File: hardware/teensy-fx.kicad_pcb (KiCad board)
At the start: 4 copper layers, 60 x 100 mm, 79 parts, among them J1 AudioJack3_Ground, J2 AudioJack3_Ground, J3 AudioJack3_Ground, SW1 Switch_SW_Push, SW2 Switch_SW_Push, SW3 Switch_SW_Push, SW4 Switch_SW_Push, U1 Teensy4.0, U2 AP7313-1.8V, U3 SGTL5000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

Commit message: try adding resistors to all the i2s lines
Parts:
- added RN1: R_Pack04, Resistor_SMD:R_Array_Convex_4x0603, F.Cu at (251.6, 55.2)
- moved R3 4.53 mm to (244.9, 54.0)
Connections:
- U3 pad 23: LRCLK -> Net-(RN1-Pad8)
- U3 pad 24: BCLK -> Net-(RN1-Pad7)
- U3 pad 25: I2S_IN -> Net-(RN1-Pad6)
- U3 pad 26: I2S_OUT -> Net-(RN1-Pad5)
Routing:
- net BCLK: track 17.8 -> 13.0 mm, vias 2 -> 0
- net LRCLK: track 17.6 -> 12.9 mm
- net MCLK: track 16.0 -> 11.9 mm
- net Net-(RN1-Pad5): track 0.00 -> 3.49 mm
- net Net-(R3-Pad1): track 5.99 -> 9.46 mm
- net Net-(RN1-Pad8): track 0.00 -> 3.46 mm
- net I2S_OUT: track 27.4 -> 24.0 mm
- net Net-(RN1-Pad7): track 0.00 -> 3.03 mm
- net Net-(RN1-Pad6): track 0.00 -> 2.95 mm
- net I2S_IN: track 22.2 -> 19.3 mm

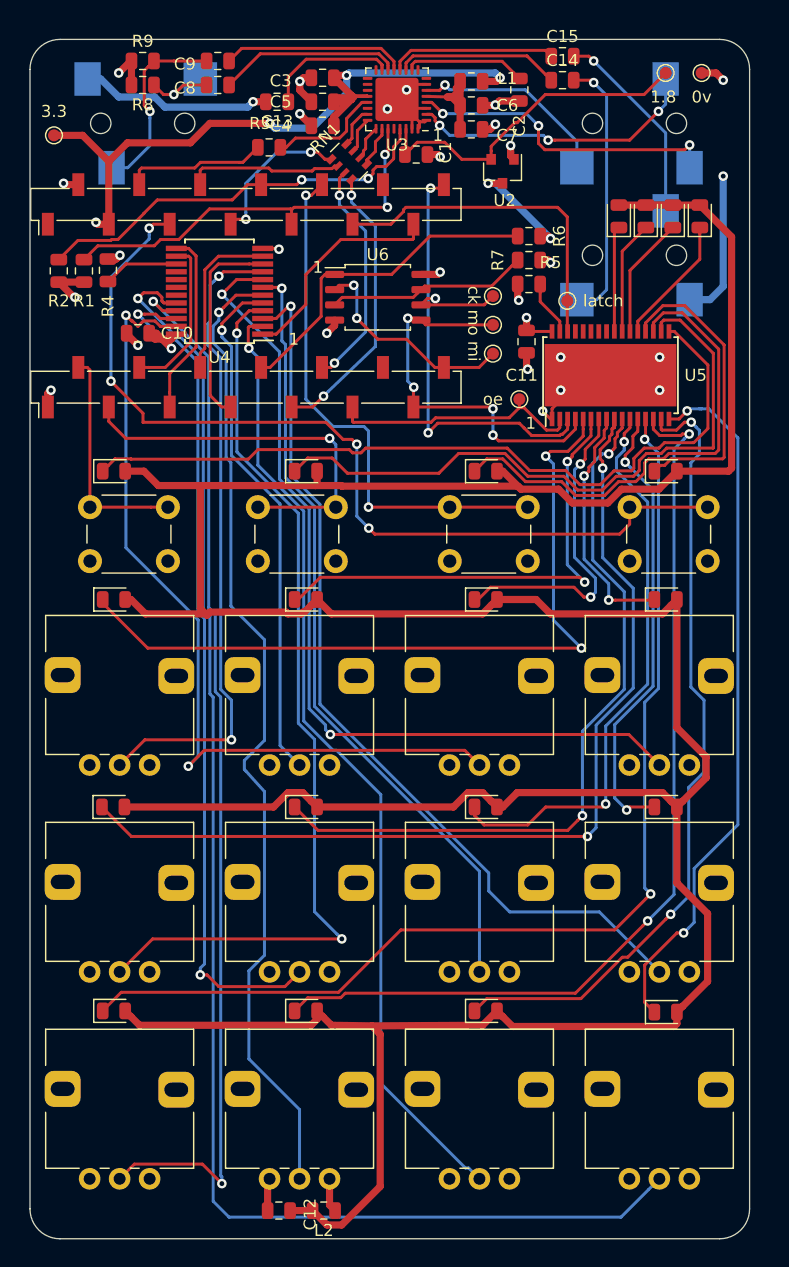
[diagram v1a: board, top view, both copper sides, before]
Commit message: change 3v3 plane to gnd, route all i2s signals on top plane, add rc filter for ADC pot input
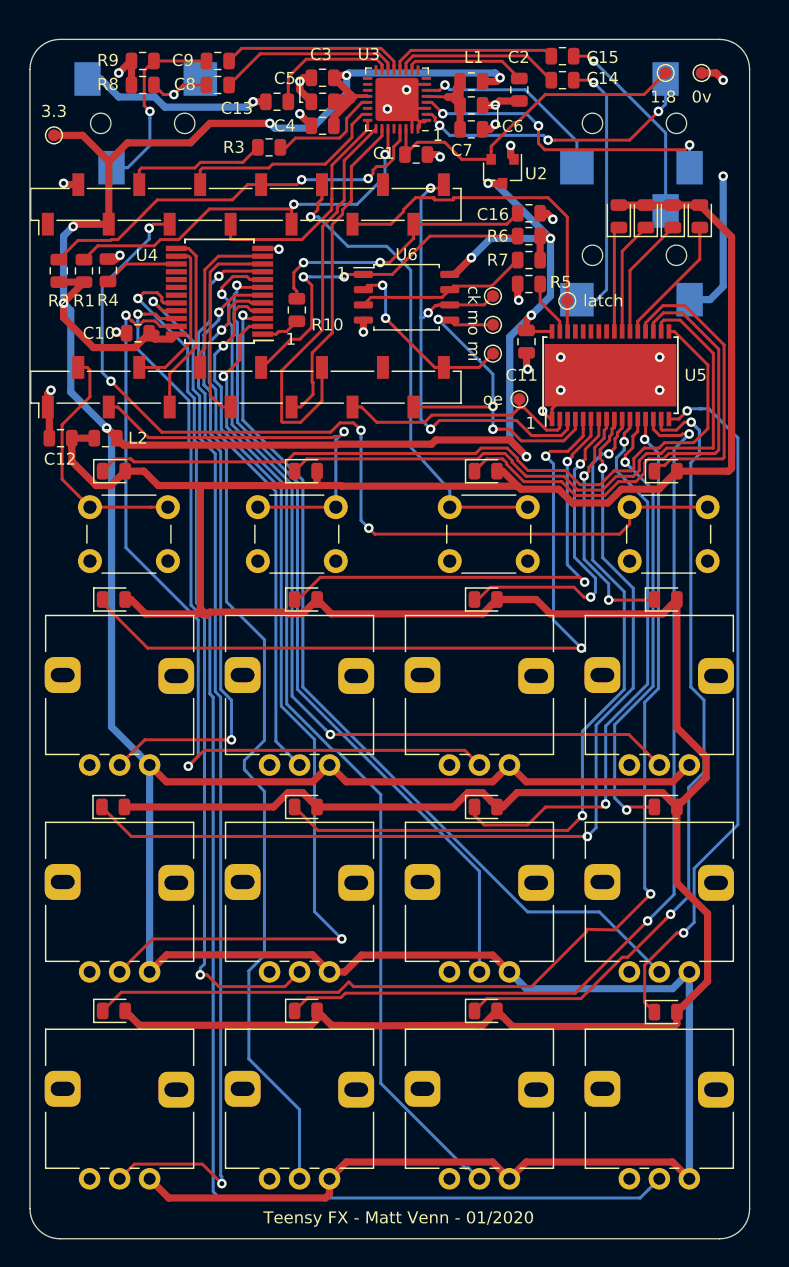
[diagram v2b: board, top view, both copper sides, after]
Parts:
- removed RN1: R_Pack04, Resistor_SMD:R_Array_Convex_4x0603
- added C16: 2.2uF, Capacitor_SMD:C_0805_2012Metric, F.Cu at (266.6, 59.5)
- added R10: 200r, Resistor_SMD:R_0805_2012Metric, F.Cu at (247.2, 67.6)
- moved C12 66.9 mm to (227.6, 78.2)
- moved L2 66.9 mm to (231.3, 78.2)
- moved U6 2.40 mm to (256.4, 66.5)
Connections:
- U3 pad 23: Net-(RN1-Pad8) -> BCLK
- U3 pad 24: Net-(RN1-Pad7) -> LRCLK
- U3 pad 25: Net-(RN1-Pad6) -> I2S_IN
- U3 pad 26: Net-(RN1-Pad5) -> I2S_OUT
- U4 pad 1: pot_multiplex -> Net-(R10-Pad1)
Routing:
- net +3V3: track 100.1 -> 395.9 mm
- net I2S_IN: track 19.3 -> 34.6 mm, vias 2 -> 0
- net +3.3VA: track 307.1 -> 293.7 mm
- net LRCLK: track 12.9 -> 19.4 mm, vias 2 -> 0
- net pot_multiplex: track 18.7 -> 23.7 mm, vias 0 -> 2
- net BCLK: track 13.0 -> 17.7 mm
- net sw_3: track 44.7 -> 40.8 mm, vias 2 -> 1
- net Net-(RN1-Pad5): track 3.49 -> 0.00 mm
- net Net-(R10-Pad1): track 0.00 -> 3.47 mm
- net Net-(RN1-Pad8): track 3.46 -> 0.00 mm
- net Net-(RN1-Pad7): track 3.03 -> 0.00 mm
- net Net-(RN1-Pad6): track 2.95 -> 0.00 mm
- net I2S_OUT: track 24.0 -> 26.8 mm, vias 2 -> 0
- net /pots buttons & LEDs/a2: track 65.5 -> 68.0 mm
- net /pots buttons & LEDs/a5: track 77.2 -> 79.8 mm
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- removed copper zone on In2.Cu, net +3V3
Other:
- board text added: "Teensy FX - Matt Venn - 01/2020"

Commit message: notes, check current, add extra decoupling cap for reg, move led supply to 5v
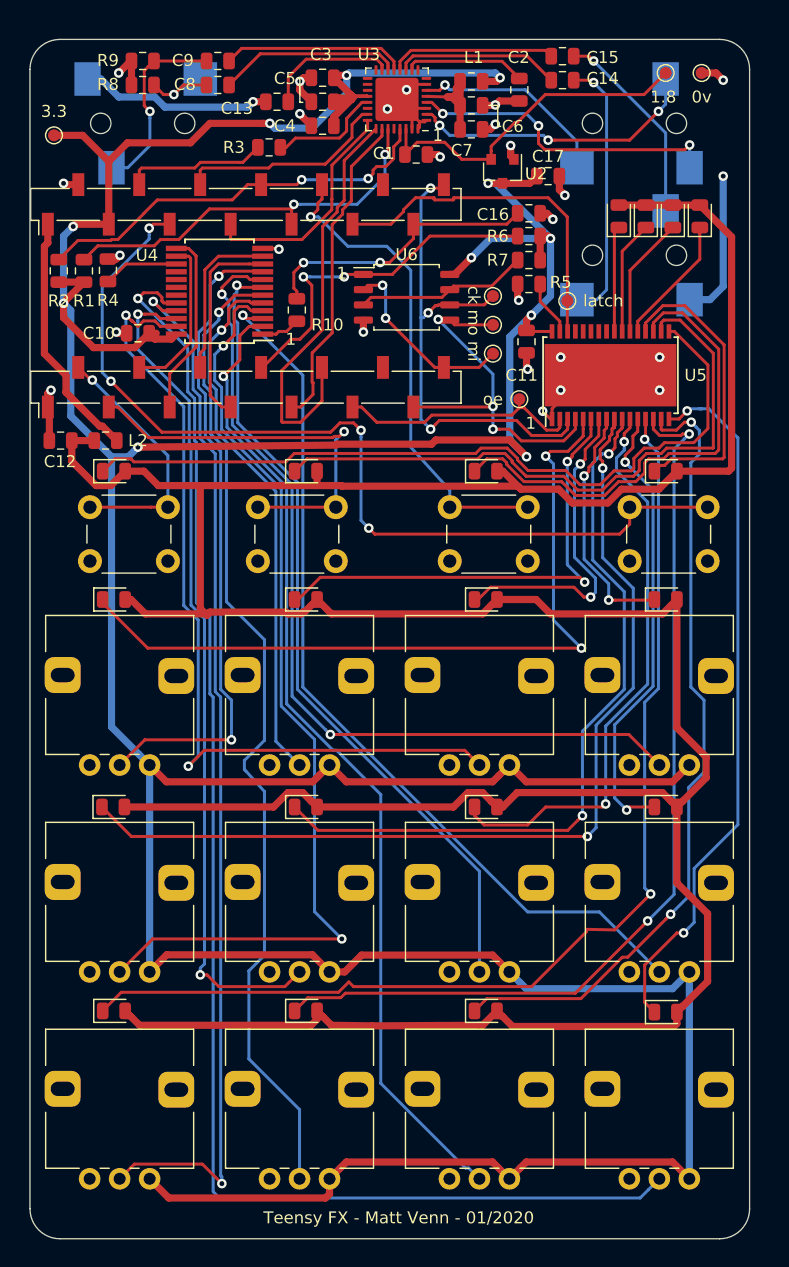
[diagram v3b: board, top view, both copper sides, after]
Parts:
- added C17: 2.2uF, Capacitor_SMD:C_0805_2012Metric, F.Cu at (268.2, 56.4)
- R5: value 3.3k -> 5k
- moved C12 0.20 mm to (227.6, 78.5)
- moved L2 0.20 mm to (231.3, 78.5)
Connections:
- net +3.3VA renamed +5VA
- L2 pad 1: +3V3 -> +5V
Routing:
- net +5V: track 0.00 -> 20.8 mm
- net +3V3: track 395.9 -> 398.3 mm
- net GND: track 80.3 -> 82.1 mm, vias 26 -> 27
- net sw_1: track 20.9 -> 21.3 mm, vias 0 -> 1

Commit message: fix teensy smt fp for molex part
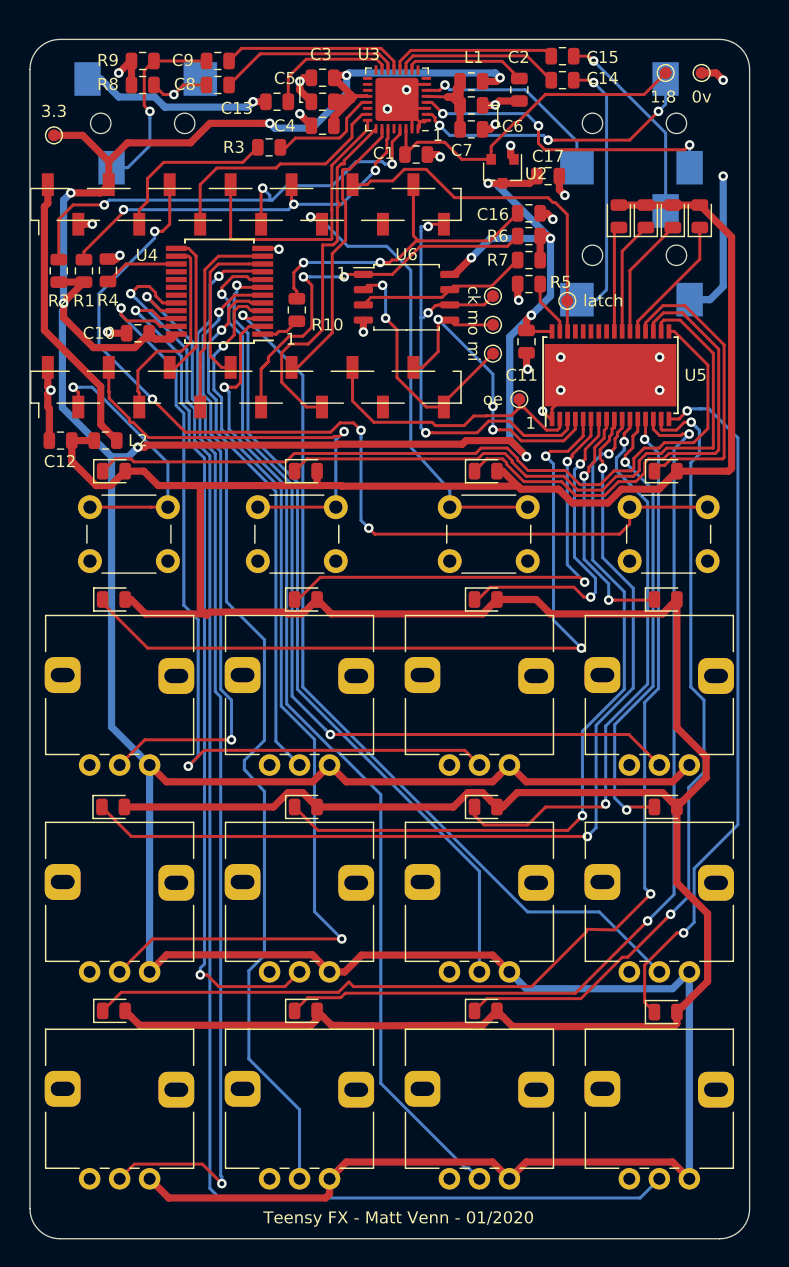
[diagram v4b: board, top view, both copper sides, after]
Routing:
- net SCL: track 34.3 -> 40.8 mm, vias 2 -> 3
- net MISO: track 15.7 -> 21.0 mm
- net LRCLK: track 19.4 -> 24.1 mm
- net pot_multiplex: track 23.7 -> 27.9 mm
- net I2S_IN: track 34.6 -> 30.4 mm
- net /mem_cs: track 29.4 -> 33.5 mm
- net pot_b2: track 13.4 -> 16.7 mm
- net pot_b1: track 13.6 -> 16.9 mm
- net pot_b0: track 17.0 -> 13.7 mm
- net led_oe: track 20.6 -> 23.8 mm
- net +5V: track 20.8 -> 24.0 mm
- net sw_2: track 34.0 -> 37.0 mm
- net pot_b3: track 15.4 -> 12.6 mm
- net I2S_OUT: track 26.8 -> 24.0 mm
- net GND: track 82.1 -> 84.8 mm
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
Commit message: footprints
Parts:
- C14, C15, C8, C9: value 2.2uF -> 1uF; footprint Capacitor_SMD:C_0805_2012Metric -> Capacitor_SMD:C_1210_3225Metric
- J1, J2, J3: footprint Connector_Audio:Jack_3.5mm_CUI_SJ-3523-SMT_Horizontal -> audio-fx:Jack_3.5mm_CUI_SJ-3523-SMT_Horizontal
- moved TP6 6.58 mm to (233.5, 52.0)
- moved C15 6.14 mm to (275.2, 48.4), turned to 270 degrees
- moved C14 2.40 mm to (271.8, 48.4), turned to 270 degrees
- moved C8 1.85 mm to (241.6, 50.4)
- moved C9 1.02 mm to (241.6, 47.2)
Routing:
- net LRCLK: track 24.1 -> 14.2 mm
- net Net-(C15-Pad1): track 13.9 -> 20.9 mm
- net Net-(C15-Pad2): track 16.8 -> 10.7 mm
- net /pots buttons & LEDs/a5: track 79.8 -> 74.8 mm
- net GND: track 84.8 -> 87.8 mm
- net Net-(C14-Pad1): track 13.8 -> 16.5 mm
- net Net-(C14-Pad2): track 22.3 -> 19.7 mm
- net Net-(C9-Pad1): track 15.4 -> 14.1 mm
- net /pots buttons & LEDs/a10: track 89.2 -> 90.3 mm
- net /pots buttons & LEDs/a3: track 82.8 -> 83.9 mm
- net /pots buttons & LEDs/a7: track 82.8 -> 83.8 mm
- net +5VA: track 293.7 -> 294.6 mm
- net Net-(D6-Pad1): track 62.3 -> 63.1 mm
- net /pots buttons & LEDs/a8: track 72.1 -> 72.8 mm
- net Net-(C9-Pad2): track 15.9 -> 16.6 mm
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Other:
- board text added: "$git$"
- board text added: "0123"
- board text added: "in"
- board text added: "line"
- board text added: "phones"

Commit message: ready to order
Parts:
- added G***: LOGO, audio-fx:back-graphic, B.Cu at (255.0, 111.4)
- added G***: LOGO, audio-fx:back-graphic, F.Cu at (255.0, 111.5)
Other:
- board text added: "Art by Kipling http://bit.ly/39Wxc4R"
- board text added: "http://bit.ly/teensy-fx"
- board text added: "startshape START size { s 2.2} background { b -.5} rule START{ 2* {s -1} SQUARE [ s 1.1 x .5 y .5 z -5] 2* {s -1} SQUARE [ s 1.1 x .5 y -.5 z -5 b 1] 2* {s -1} CIRCLE [ x 1.2 z -4 s .5] 2* {s -1} CIRCLE [ y 1.2 z -4 s .5 b 1] CIRCLE { z -3 b .8 } S{ |sat .26 h -60} } rule S { FOUR{} S{ r .9 s .999 sat .0005| h 1.1 b .0002} } rule S 0.002{ W{}} rule W { 12* { r .9 s .999 h 1.1} FOUR{r 90 z -1 h 90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"

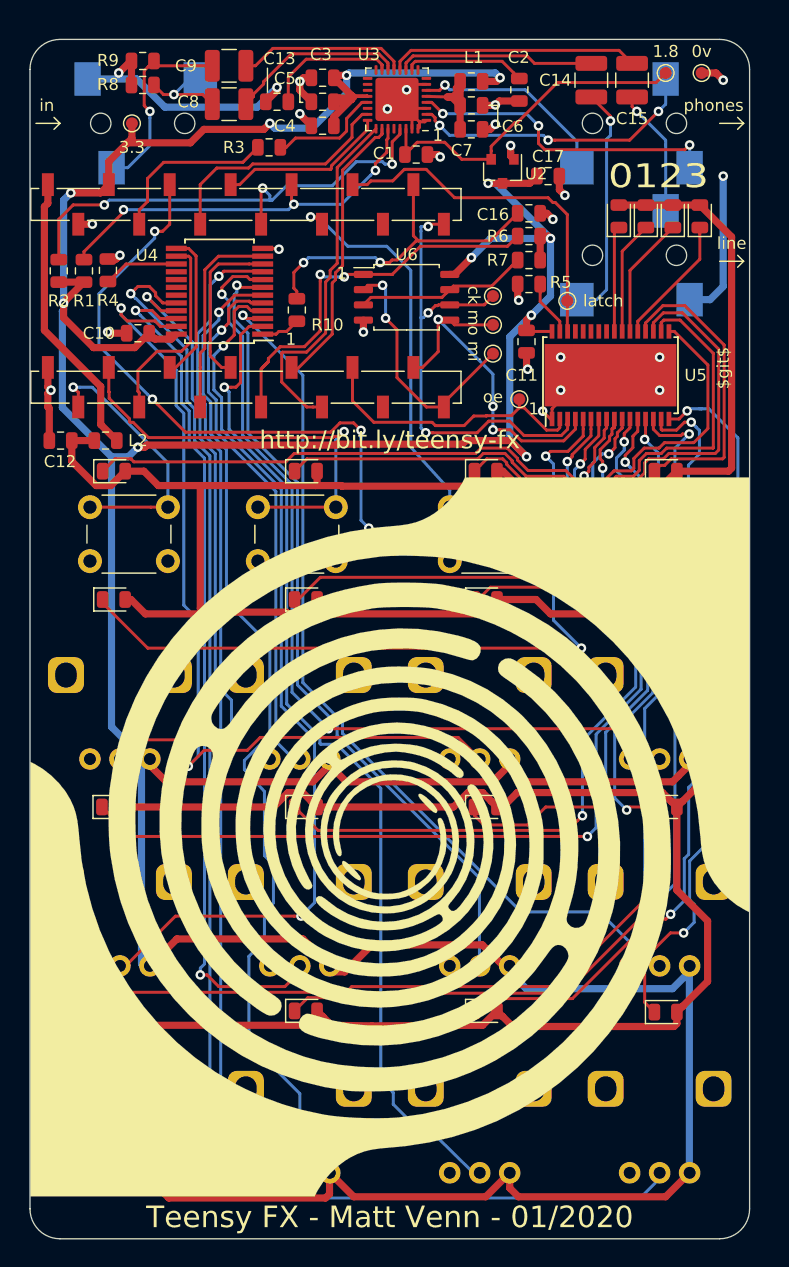
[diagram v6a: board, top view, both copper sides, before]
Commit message: slightly improve ground layer by moving vias
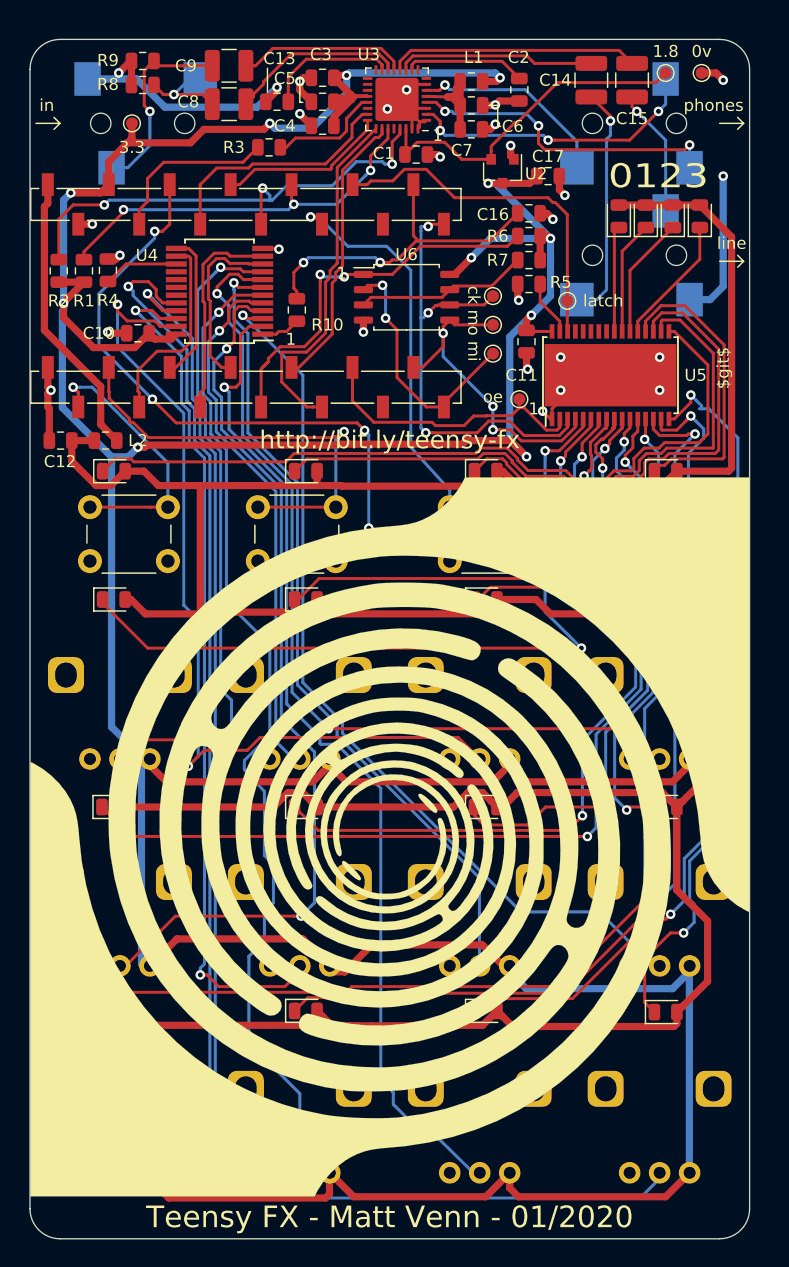
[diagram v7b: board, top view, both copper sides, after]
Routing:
- net MOSI: track 29.7 -> 27.6 mm
- net Net-(D12-Pad1): track 59.7 -> 61.2 mm
- net /pots buttons & LEDs/a11: track 120.6 -> 121.7 mm
- net Net-(D11-Pad1): track 66.9 -> 67.9 mm
- net pot_b0: track 13.7 -> 14.6 mm
- net /pots buttons & LEDs/a8: track 72.8 -> 73.7 mm
- net /pots buttons & LEDs/a1: track 73.2 -> 74.0 mm
- net Net-(D10-Pad1): track 78.2 -> 78.9 mm
- net pot_b1: track 16.9 -> 17.6 mm
- net /pots buttons & LEDs/a0: track 54.6 -> 55.2 mm
